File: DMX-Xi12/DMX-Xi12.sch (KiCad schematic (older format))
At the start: 14 parts, among them J1 RJ45, J2 RJ45, U1 MAX13450E, U2 4N25, U3 4N25, U4 4N25

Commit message: finished input stage and started work on processor stage
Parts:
- removed C1, C2: 0.1uF, symbol CP
- removed J1, J2: RJ45, symbol RJ45
- removed R1, R4, R6: 190R, symbol R
- removed R2, R3, R5: 500R, symbol R
- removed U1: MAX13450E, TSSOP-14EP, symbol MAX13450E
- removed U2, U3, U4: 4N25, DIP-6, symbol 4N25
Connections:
- net labels removed: +5V, GND, RX, RX_ENABLE, TX_ENABLE
- wire segments 55 -> 0

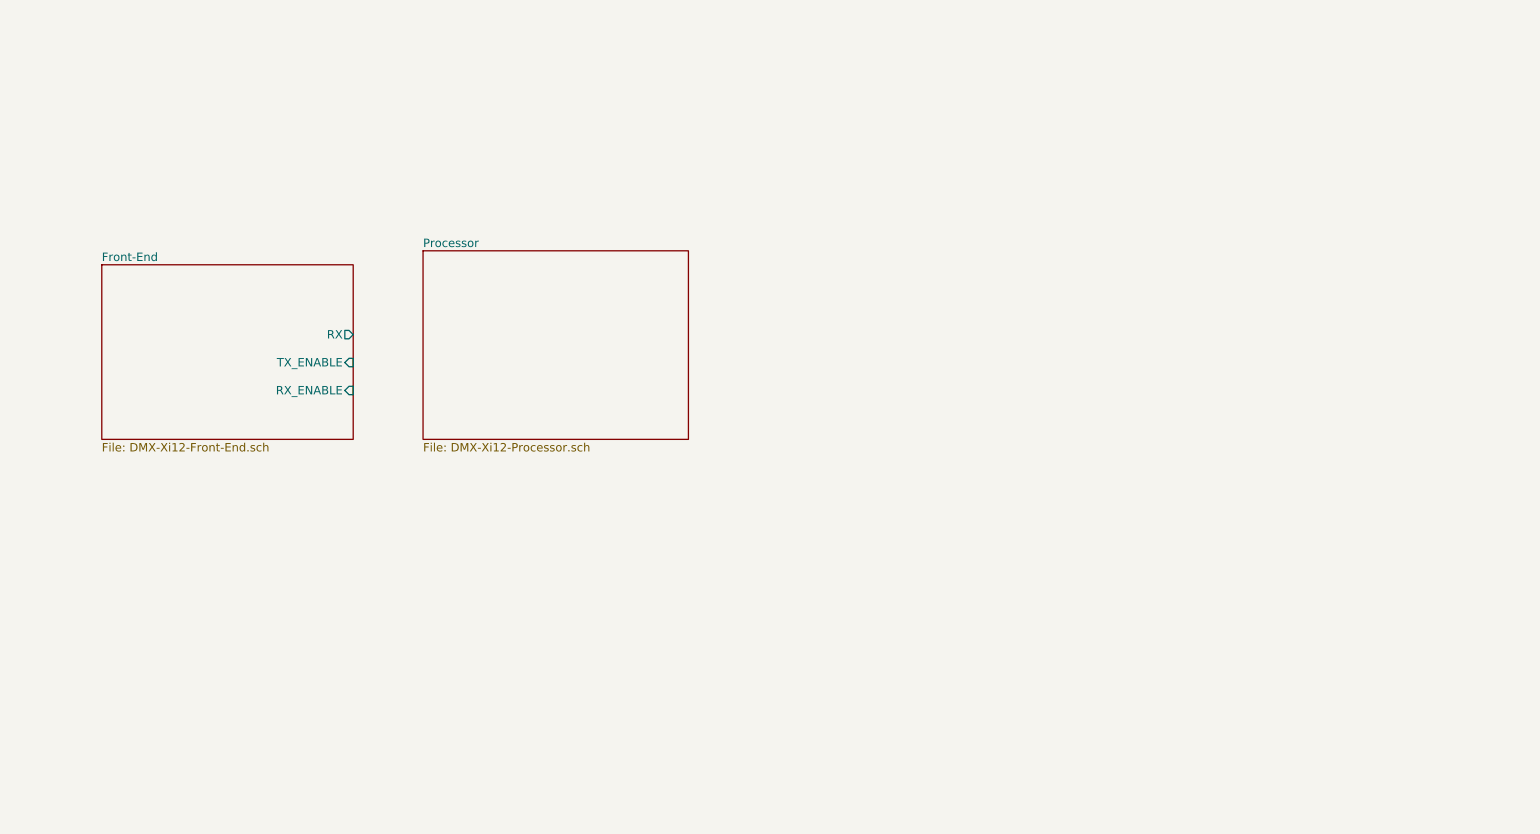
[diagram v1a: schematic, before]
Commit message: added output stage
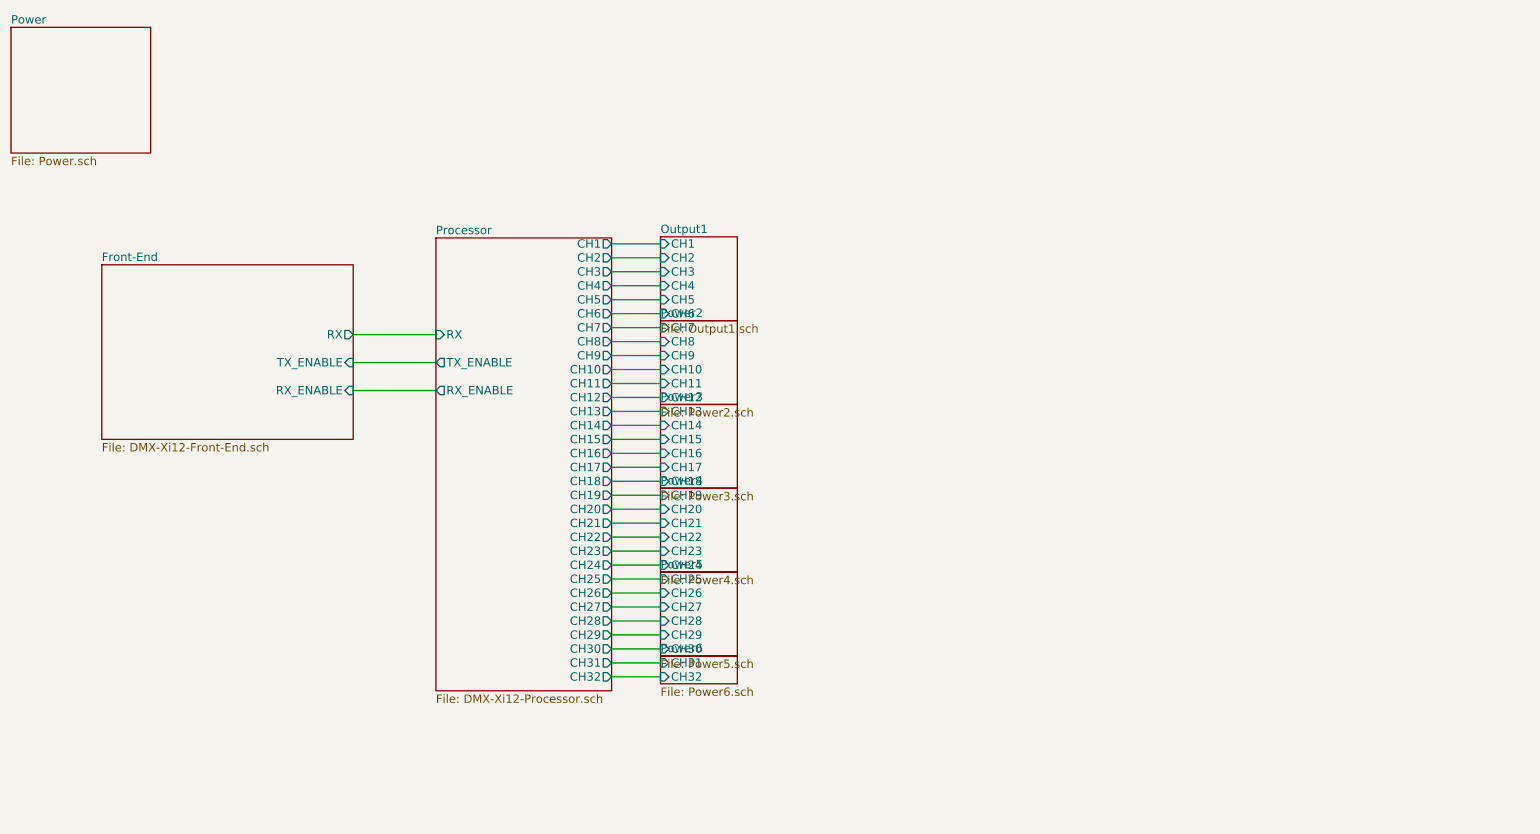
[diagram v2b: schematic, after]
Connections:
- wire segments 0 -> 35
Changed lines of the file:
@@
 LIBS:valves
 LIBS:DMX-Xi12
+LIBS:dips-s
+LIBS:MyPower
 LIBS:DMX-Xi12-cache
 EELAYER 25 0
@@
 $Descr A4 11693 8268
 encoding utf-8
-Sheet 1 3
+Sheet 1 10
 Title "DMX-Xi12"
 Date ""
@@
 $EndSheet
 $Sheet
-S 3950 2600 1900 1350
+S 4042 2508 1258 3242
 U 56AE176E
 F0 "Processor" 60
 F1 "DMX-Xi12-Processor.sch" 60
-$EndSheet
+F2 "CH3" O R 5300 2750 60
+F3 "CH4" O R 5300 2850 60
+F4 "CH1" O R 5300 2550 60
+F5 "CH2" O R 5300 2650 60
+F6 "CH7" O R 5300 3150 60
+F7 "CH8" O R 5300 3250 60
+F8 "CH5" O R 5300 2950 60
+F9 "CH6" O R 5300 3050 60
+F10 "CH10" O R 5300 3450 60
+F11 "CH11" O R 5300 3550 60
+F12 "CH9" O R 5300 3350 60
+F13 "CH14" O R 5300 3850 60
+F14 "CH15" O R 5300 3950 60
+F15 "CH12" O R 5300 3650 60
+F16 "CH13" O R 5300 3750 60
+F17 "CH18" O R 5300 4250 60
+F18 "CH19" O R 5300 4350 60
+F19 "CH16" O R 5300 4050 60
+F20 "CH17" O R 5300 4150 60
+F21 "CH22" O R 5300 4650 60
+F22 "CH23" O R 5300 4750 60
+F23 "CH20" O R 5300 4450 60
+F24 "CH21" O R 5300 4550 60
+F25 "CH26" O R 5300 5050 60
+F26 "CH27" O R 5300 5150 60
+F27 "CH24" O R 5300 4850 60
+F28 "CH25" O R 5300 4950 60
+F29 "CH30" O R 5300 5450 60
+F30 "CH31" O R 5300 5550 60
+F31 "CH28" O R 5300 5250 60
+F32 "CH29" O R 5300 5350 60
+F33 "CH32" O R 5300 5650 60
+F34 "RX" I L 4042 3200 60
+F35 "RX_ENABLE" O L 4042 3600 60
+F36 "TX_ENABLE" O L 4042 3400 60
+$EndSheet
+$Sheet
+S 1000 1000 1000 900
+U 56B681B8
+F0 "Power" 60
+F1 "Power.sch" 60
+$EndSheet
+$Sheet
+S 5650 3100 550  600
+U 56B6F54D
+F0 "Power2" 60
+F1 "Power2.sch" 60
+F2 "CH7" I L 5650 3150 60
+F3 "CH8" I L 5650 3250 60
+F4 "CH9" I L 5650 3350 60
+F5 "CH10" I L 5650 3450 60
+F6 "CH11" I L 5650 3550 60
+F7 "CH12" I L 5650 3650 60
+$EndSheet
+$Sheet
+S 5650 2500 550  600
+U 56B68A68
+F0 "Output1" 60
+F1 "Output1.sch" 60
+F2 "CH1" I L 5650 2550 60
+F3 "CH2" I L 5650 2650 60
+F4 "CH3" I L 5650 2750 60
+F5 "CH4" I L 5650 2850 60
+F6 "CH5" I L 5650 2950 60
+F7 "CH6" I L 5650 3050 60
+$EndSheet
+$Sheet
+S 5650 3700 550  600
+U 56B849B3
+F0 "Power3" 60
+F1 "Power3.sch" 60
+F2 "CH13" I L 5650 3750 60
+F3 "CH14" I L 5650 3850 60
+F4 "CH15" I L 5650 3950 60
+F5 "CH16" I L 5650 4050 60
+F6 "CH17" I L 5650 4150 60
+F7 "CH18" I L 5650 4250 60
+$EndSheet
+$Sheet
+S 5650 4300 550  600
+U 56B8C27D
+F0 "Power4" 60
+F1 "Power4.sch" 60
+F2 "CH19" I L 5650 4350 60
+F3 "CH20" I L 5650 4450 60
+F4 "CH21" I L 5650 4550 60
+F5 "CH22" I L 5650 4650 60
+F6 "CH23" I L 5650 4750 60
+F7 "CH24" I L 5650 4850 60
+$EndSheet
+$Sheet
+S 5650 4900 550  600
+U 56B974A4
+F0 "Power5" 60
+F1 "Power5.sch" 60
+F2 "CH25" I L 5650 4950 60
+F3 "CH26" I L 5650 5050 60
+F4 "CH27" I L 5650 5150 60
+F5 "CH28" I L 5650 5250 60
+F6 "CH29" I L 5650 5350 60
+F7 "CH30" I L 5650 5450 60
+$EndSheet
+$Sheet
+S 5650 5500 550  200
+U 56B991B6
+F0 "Power6" 60
+F1 "Power6.sch" 60
+F2 "CH31" I L 5650 5550 60
+F3 "CH32" I L 5650 5650 60
+$EndSheet
+Wire Wire Line
+	4050 3200 3450 3200
+Wire Wire Line
+	4050 3600 3450 3600
+Wire Wire Line
+	4050 3400 3450 3400
+Wire Wire Line
+	5300 2550 5650 2550
+Wire Wire Line
+	5300 2650 5650 2650
+Wire Wire Line
+	5650 2750 5300 2750
+Wire Wire Line
+	5300 2850 5650 2850
+Wire Wire Line
+	5300 2950 5650 2950
+Wire Wire Line
+	5300 3050 5650 3050
+Wire Wire Line
+	5650 3150 5300 3150
+Wire Wire Line
+	5300 3250 5650 3250
+Wire Wire Line
+	5650 3350 5300 3350
+Wire Wire Line
+	5300 3450 5650 3450
+Wire Wire Line
+	5650 3550 5300 3550
+Wire Wire Line
+	5300 3650 5650 3650
+Wire Wire Line
+	5650 3750 5300 3750
+Wire Wire Line
+	5300 3850 5650 3850
+Wire Wire Line
+	5650 3950 5300 3950
+Wire Wire Line
+	5300 4050 5650 4050
+Wire Wire Line
+	5650 4150 5300 4150
+Wire Wire Line
+	5300 4250 5650 4250
+Wire Wire Line
+	5650 4350 5300 4350
+Wire Wire Line
+	5300 4450 5650 4450
+Wire Wire Line
+	5300 4550 5650 4550
+Wire Wire Line
+	5650 4650 5300 4650
+Wire Wire Line
+	5300 4750 5650 4750
+Wire Wire Line
+	5650 4850 5300 4850
+Wire Wire Line
+	5300 4950 5650 4950
+Wire Wire Line
+	5650 5050 5300 5050
+Wire Wire Line
+	5300 5150 5650 5150
+Wire Wire Line
+	5650 5250 5300 5250
+Wire Wire Line
+	5300 5350 5650 5350
+Wire Wire Line
+	5650 5450 5300 5450
+Wire Wire Line
+	5300 5550 5650 5550
+Wire Wire Line
+	5650 5650 5300 5650
 $EndSCHEMATC

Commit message: more schematic
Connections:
- wire segments 35 -> 38
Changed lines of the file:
@@
 F35 "RX_ENABLE" O L 4042 3600 60
 F36 "TX_ENABLE" O L 4042 3400 60
+F37 "Zero_crossing" O L 4042 3000 60
 $EndSheet
 $Sheet
@@
 F0 "Power" 60
 F1 "Power.sch" 60
+F2 "Zero_crossing" O R 2000 1450 60
 $EndSheet
 $Sheet
@@
 Wire Wire Line
 	5650 5650 5300 5650
+Wire Wire Line
+	4050 3000 3550 3000
+Wire Wire Line
+	3550 3000 3550 1450
+Wire Wire Line
+	3550 1450 2000 1450
 $EndSCHEMATC

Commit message: made dlaw changes etc
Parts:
- added P? (x2): CONN_01X17, symbol CONN_01X17
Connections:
- net labels added: LiveA, LiveB, NeutralA, NeutralB
- wire segments 38 -> 83

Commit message: working on pcb
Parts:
- removed P? (x2): CONN_01X17, symbol CONN_01X17
- added Con10, Con2, Con3, Con4, Con5, Con6, Con7, Con8, Con9: Screw-terminal, Components:Screw-terminal, symbol Screw-terminal

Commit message: more work on board
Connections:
- wire segments 83 -> 85
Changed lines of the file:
@@
 Wire Wire Line
 	6350 5650 6550 5650
-Wire Wire Line
-	6550 5750 6350 5750
 $Comp
 L Screw-terminal Con2
@@
 	8900 6300 6450 6300
 Wire Wire Line
-	6450 6300 6450 6050
+	6450 6300 6450 5750
 Wire Wire Line
-	6450 6050 6550 6050
+	6450 5750 6550 5750
+Wire Wire Line
+	6350 5750 6400 5750
+Wire Wire Line
+	6400 5750 6400 6050
+Wire Wire Line
+	6400 6050 6550 6050
 $EndSCHEMATC

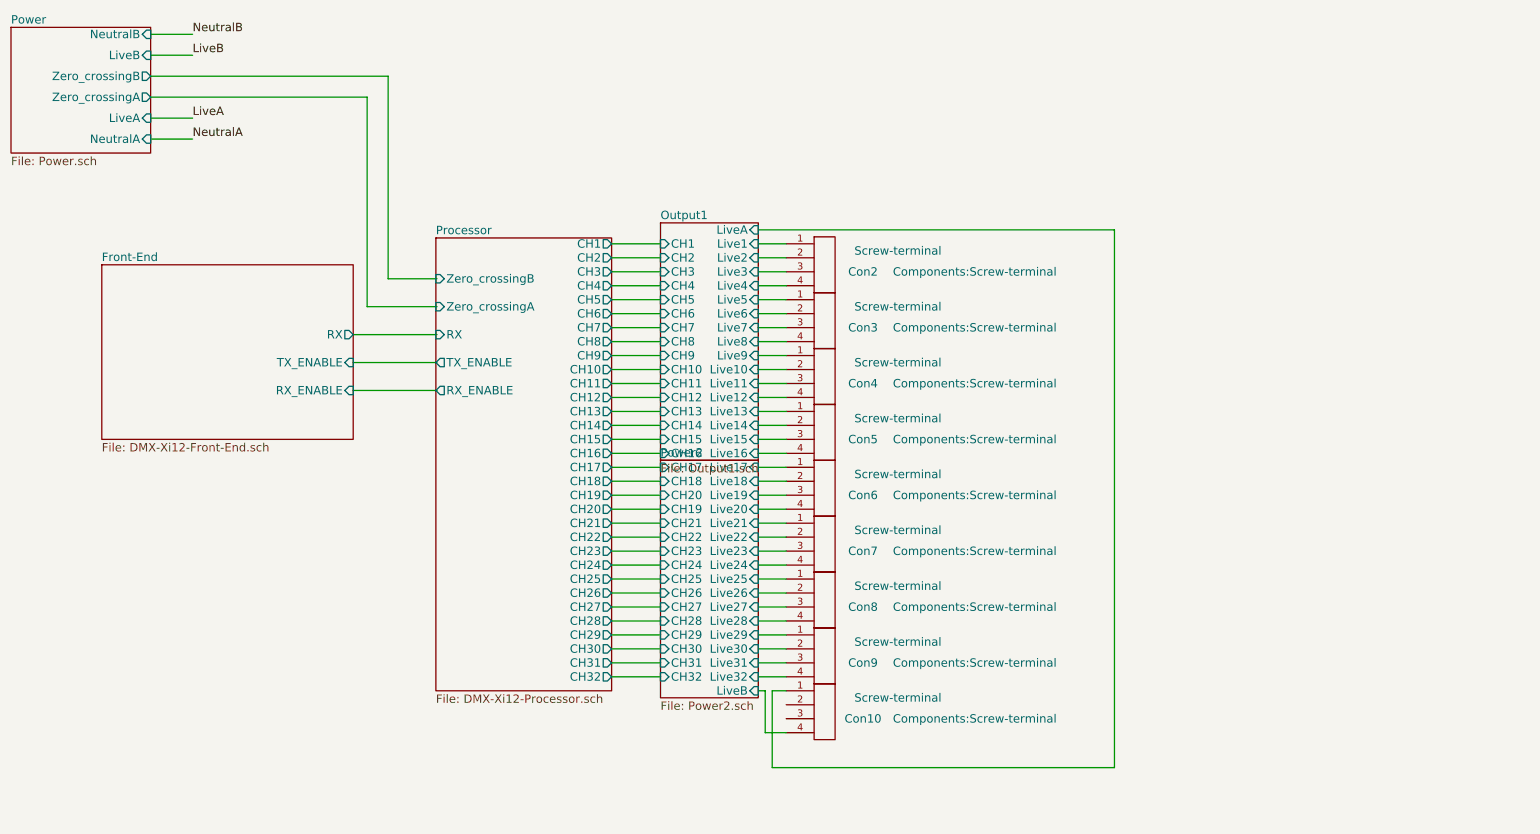
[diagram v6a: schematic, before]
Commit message: completed board. Schematic, is correct but some part values and numbers need updating! Do not trust the schematic yet
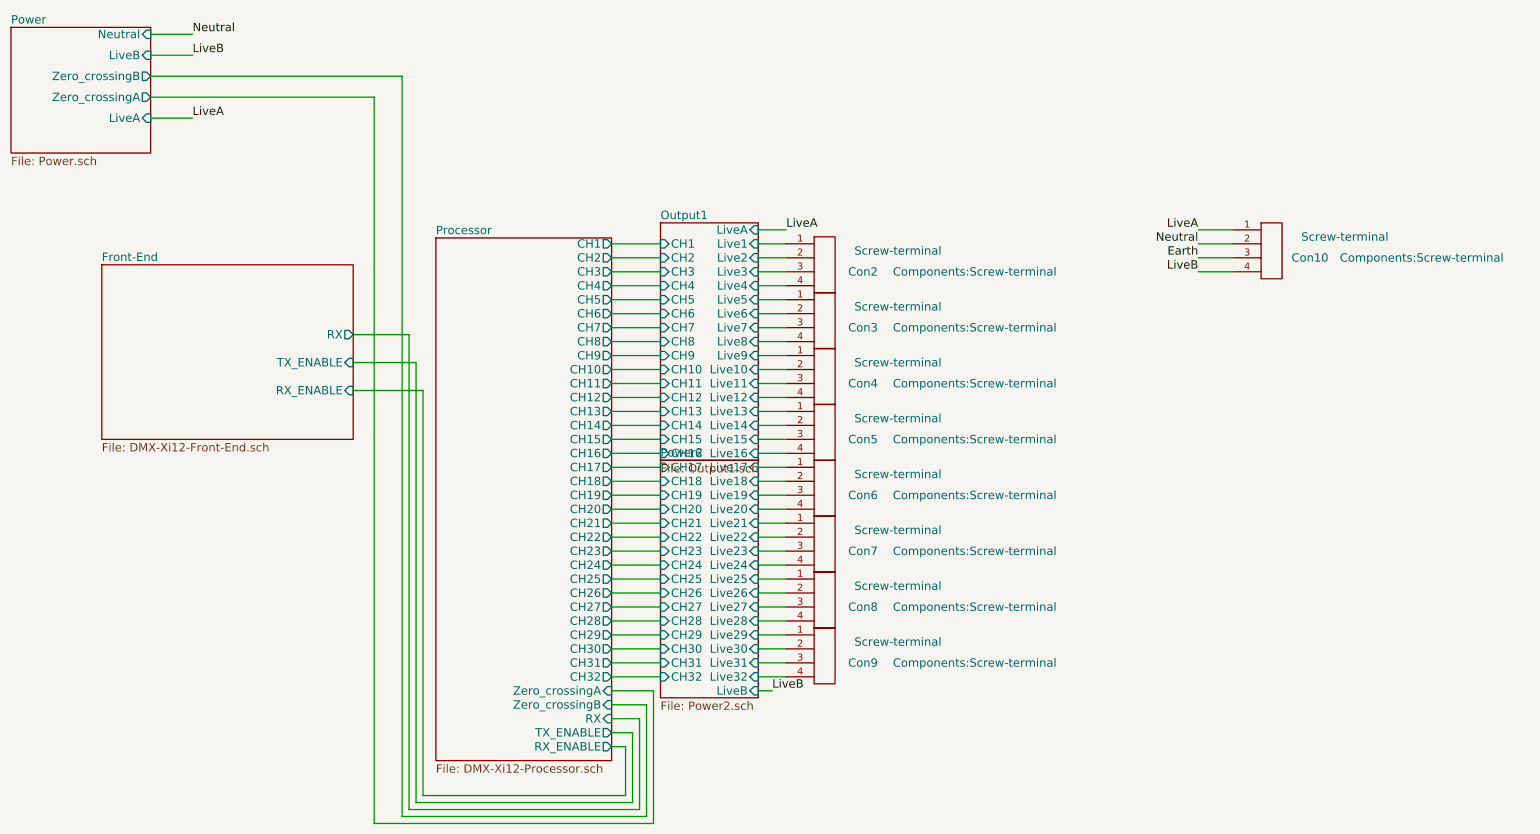
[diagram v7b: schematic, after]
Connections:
- net labels added: Earth, Neutral
- net labels removed: NeutralA, NeutralB
- wire segments 85 -> 98
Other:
- moved on the sheet: Con10
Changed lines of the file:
@@
 $EndSheet
 $Sheet
-S 4042 2508 1258 3242
+S 4042 2508 1258 3742
 U 56AE176E
 F0 "Processor" 60
@@
 F32 "CH29" O R 5300 5350 60
 F33 "CH32" O R 5300 5650 60
-F34 "RX" I L 4042 3200 60
-F35 "RX_ENABLE" O L 4042 3600 60
-F36 "TX_ENABLE" O L 4042 3400 60
-F37 "Zero_crossingA" I L 4042 3000 60
-F38 "Zero_crossingB" I L 4042 2800 60
+F34 "RX" I R 5300 5950 60
+F35 "RX_ENABLE" O R 5300 6150 60
+F36 "TX_ENABLE" O R 5300 6050 60
+F37 "Zero_crossingA" I R 5300 5750 60
+F38 "Zero_crossingB" I R 5300 5850 60
 $EndSheet
 $Sheet
@@
 F4 "LiveA" I R 2000 1650 60
 F5 "LiveB" I R 2000 1200 60
-F6 "NeutralA" I R 2000 1800 60
-F7 "NeutralB" I R 2000 1050 60
+F6 "Neutral" I R 2000 1050 60
 $EndSheet
-Text Label 2300 1800 0    60   ~ 0
-NeutralA
 Text Label 2300 1650 0    60   ~ 0
 LiveA
 Text Label 2300 1200 0    60   ~ 0
 LiveB
-Text Label 2300 1050 0    60   ~ 0
-NeutralB
 $Sheet
 S 5650 4100 700  1700
@@
 F2 "CH18" I L 5650 4250 60
 F3 "CH17" I L 5650 4150 60
-F4 "CH20" I L 5650 4350 60
-F5 "CH19" I L 5650 4450 60
+F4 "CH20" I L 5650 4450 60
+F5 "CH19" I L 5650 4350 60
 F6 "CH22" I L 5650 4650 60
 F7 "CH21" I L 5650 4550 60
@@
 $EndSheet
 Wire Wire Line
-	4050 3200 3450 3200
-Wire Wire Line
-	4050 3600 3450 3600
-Wire Wire Line
-	4050 3400 3450 3400
-Wire Wire Line
 	5300 2550 5650 2550
 Wire Wire Line
@@
 Wire Wire Line
 	5650 5650 5300 5650
-Wire Wire Line
-	4050 3000 3550 3000
-Wire Wire Line
-	4050 2800 3700 2800
-Wire Wire Line
-	2000 1500 3550 1500
-Wire Wire Line
-	3700 1350 2000 1350
-Wire Wire Line
-	3700 2800 3700 1350
-Wire Wire Line
-	3550 1500 3550 3000
-Wire Wire Line
-	2300 1800 2000 1800
 Wire Wire Line
 	2000 1050 2300 1050
@@
 F34 "LiveA" I R 6350 2450 60
 $EndSheet
-Wire Wire Line
-	6350 2450 8900 2450
 $Comp
 L Screw-terminal Con3
@@
 L Screw-terminal Con10
 U 1 1 570B2655
-P 6750 5900
-F 0 "Con10" H 7100 5850 60  0000 C CNN
-F 1 "Screw-terminal" H 7350 6000 60  0000 C CNN
-F 2 "Components:Screw-terminal" H 7900 5850 60  0000 C CNN
-F 3 "" H 6900 5900 60  0000 C CNN
-	1    6750 5900
-	1    0    0    -1
-$EndComp
-Wire Wire Line
-	8900 2450 8900 6300
-Wire Wire Line
-	8900 6300 6450 6300
-Wire Wire Line
-	6450 6300 6450 5750
-Wire Wire Line
-	6450 5750 6550 5750
-Wire Wire Line
-	6350 5750 6400 5750
-Wire Wire Line
-	6400 5750 6400 6050
-Wire Wire Line
-	6400 6050 6550 6050
+P 9950 2600
+F 0 "Con10" H 10300 2550 60  0000 C CNN
+F 1 "Screw-terminal" H 10550 2700 60  0000 C CNN
+F 2 "Components:Screw-terminal" H 11100 2550 60  0000 C CNN
+F 3 "" H 10100 2600 60  0000 C CNN
+	1    9950 2600
+	1    0    0    -1
+$EndComp
+Text Label 9500 2550 2    60   ~ 0
+Neutral
+Wire Wire Line
+	3800 1350 3800 6650
+Wire Wire Line
+	3800 1350 2000 1350
+Wire Wire Line
+	3600 1500 3600 6700
+Wire Wire Line
+	3600 1500 2000 1500
+Wire Wire Line
+	5300 5750 5600 5750
+Wire Wire Line
+	5300 5850 5550 5850
+Wire Wire Line
+	5600 5750 5600 6700
+Wire Wire Line
+	5600 6700 3600 6700
+Wire Wire Line
+	3800 6650 5550 6650
+Wire Wire Line
+	5550 6650 5550 5850
+Wire Wire Line
+	5300 5950 5500 5950
+Wire Wire Line
+	5500 5950 5500 6600
+Wire Wire Line
+	5500 6600 3850 6600
+Wire Wire Line
+	3850 6600 3850 3200
+Wire Wire Line
+	3850 3200 3450 3200
+Wire Wire Line
+	5300 6050 5450 6050
+Wire Wire Line
+	5450 6050 5450 6550
+Wire Wire Line
+	5450 6550 3900 6550
+Wire Wire Line
+	3900 6550 3900 3400
+Wire Wire Line
+	3900 3400 3450 3400
+Wire Wire Line
+	5300 6150 5400 6150
+Wire Wire Line
+	5400 6150 5400 6500
+Wire Wire Line
+	5400 6500 3950 6500
+Wire Wire Line
+	3950 6500 3950 3600
+Wire Wire Line
+	3950 3600 3450 3600
+Text Label 6550 2450 0    60   ~ 0
+LiveA
+Text Label 9500 2750 2    60   ~ 0
+LiveB
+Wire Wire Line
+	6550 2450 6350 2450
+Text Label 9500 2450 2    60   ~ 0
+LiveA
+Wire Wire Line
+	9500 2450 9750 2450
+Wire Wire Line
+	9750 2550 9500 2550
+Wire Wire Line
+	9500 2650 9750 2650
+Wire Wire Line
+	9750 2750 9500 2750
+Text Label 6450 5750 0    60   ~ 0
+LiveB
+Wire Wire Line
+	6450 5750 6350 5750
+Text Label 2300 1050 0    60   ~ 0
+Neutral
+Text Label 9500 2650 2    60   ~ 0
+Earth
 $EndSCHEMATC
